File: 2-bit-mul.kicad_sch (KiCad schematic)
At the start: 7 parts, among them U4 SN74LS08N, U6 SN74LS08N, U7 SN74LS08N, U8 SN74HC86N

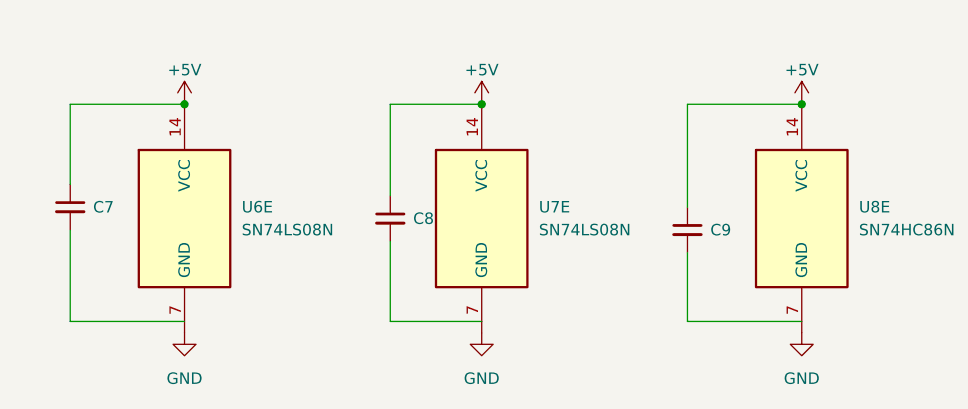
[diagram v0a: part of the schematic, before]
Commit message: fix: fixed link of capas
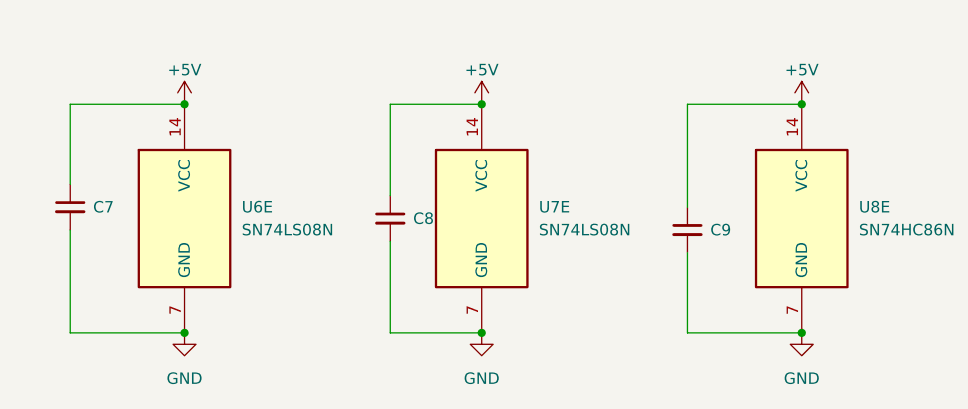
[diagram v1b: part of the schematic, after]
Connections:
- net GND: now also C7.2, C8.2, C9.2
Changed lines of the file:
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@@
+	)
+	(junction
+		(at 63.5 146.05)
+		(diameter 0)
+		(color 0 0 0 0)
 	)
 	(junction
@@
 	)
 	(junction
+		(at 96.52 146.05)
+		(diameter 0)
+		(color 0 0 0 0)
+	)
+	(junction
 		(at 132.08 120.65)
 		(diameter 0)
@@
 	(junction
 		(at 63.5 120.65)
+		(diameter 0)
+		(color 0 0 0 0)
+	)
+	(junction
+		(at 132.08 146.05)
 		(diameter 0)
 		(color 0 0 0 0)
@@
 	(wire
 		(pts
-			(xy 63.5 144.78) (xy 50.8 144.78)
+			(xy 119.38 137.16) (xy 119.38 146.05)
 		)
 		(stroke
@@
 	(wire
 		(pts
-			(xy 96.52 144.78) (xy 86.36 144.78)
-		)
-		(stroke
-			(width 0)
-			(type default)
-		)
-	)
-	(wire
-		(pts
-			(xy 119.38 144.78) (xy 119.38 137.16)
-		)
-		(stroke
-			(width 0)
-			(type default)
-		)
-	)
-	(wire
-		(pts
 			(xy 53.34 87.63) (xy 62.23 87.63)
 		)
@@
 	(wire
 		(pts
+			(xy 119.38 146.05) (xy 132.08 146.05)
+		)
+		(stroke
+			(width 0)
+			(type default)
+		)
+	)
+	(wire
+		(pts
 			(xy 63.5 93.98) (xy 67.31 93.98)
 		)
@@
 	(wire
 		(pts
-			(xy 86.36 144.78) (xy 86.36 135.89)
-		)
-		(stroke
-			(width 0)
-			(type default)
-		)
-	)
-	(wire
-		(pts
 			(xy 59.69 45.72) (xy 67.31 45.72)
 		)
@@
 	(wire
 		(pts
+			(xy 50.8 134.62) (xy 50.8 146.05)
+		)
+		(stroke
+			(width 0)
+			(type default)
+		)
+	)
+	(wire
+		(pts
 			(xy 123.19 87.63) (xy 132.08 87.63)
 		)
@@
 	(wire
 		(pts
+			(xy 86.36 135.89) (xy 86.36 146.05)
+		)
+		(stroke
+			(width 0)
+			(type default)
+		)
+	)
+	(wire
+		(pts
+			(xy 86.36 146.05) (xy 96.52 146.05)
+		)
+		(stroke
+			(width 0)
+			(type default)
+		)
+	)
+	(wire
+		(pts
 			(xy 86.36 80.01) (xy 88.9 80.01)
 		)
@@
 	(wire
 		(pts
-			(xy 132.08 144.78) (xy 119.38 144.78)
-		)
-		(stroke
-			(width 0)
-			(type default)
-		)
-	)
-	(wire
-		(pts
 			(xy 83.82 85.09) (xy 88.9 85.09)
 		)
@@
 	(wire
 		(pts
-			(xy 50.8 144.78) (xy 50.8 134.62)
-		)
-		(stroke
-			(width 0)
-			(type default)
-		)
-	)
-	(wire
-		(pts
 			(xy 62.23 40.64) (xy 67.31 40.64)
 		)
@@
 		)
 		(stroke
+			(width 0)
+			(type default)
+		)
+	)
+	(wire
+		(pts
+			(xy 50.8 146.05) (xy 63.5 146.05)
+		)
+		(stroke

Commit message: feat: updated references
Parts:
- C7, C8, C9: value C_Small -> CC0603KRX7R9BB104
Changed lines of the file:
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@@
 			)
 		)
-		(property "Value" "C_Small"
+		(property "Value" "CC0603KRX7R9BB104"
 			(at 121.92 135.8962 0)
 			(hide yes)
@@
 			)
 		)
-		(property "Value" "C_Small"
+		(property "Value" "CC0603KRX7R9BB104"
 			(at 88.9 134.6262 0)
 			(hide yes)
@@
 			)
 		)
-		(property "Value" "C_Small"
+		(property "Value" "CC0603KRX7R9BB104"
 			(at 53.34 133.3562 0)
 			(hide yes)

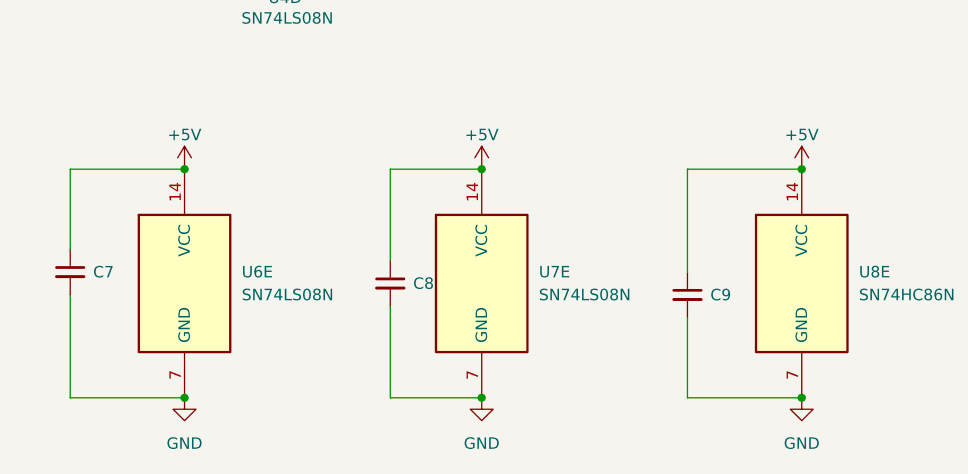
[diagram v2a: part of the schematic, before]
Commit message: Remove capacitors + change R and C footprints + finish PCB routing
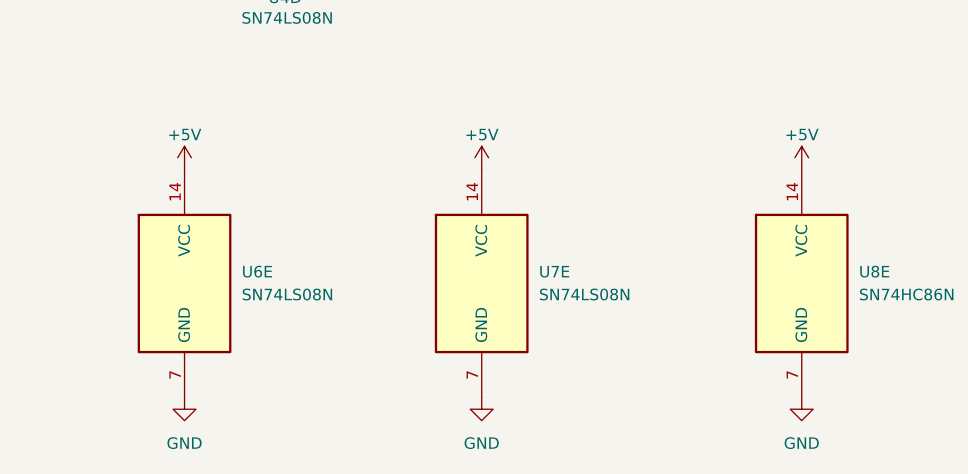
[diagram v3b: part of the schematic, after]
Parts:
- removed C7, C8, C9: CC0603KRX7R9BB104, Capacitor_SMD:C_0603_1608Metric_Pad1.08x0.95mm_HandSolder, symbol Device:C_Small

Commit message: fix: reput capas -- where is my gift?
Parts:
- added C7, C8, C9: C_Small, Capacitor_SMD:C_0603_1608Metric, symbol Device:C_Small
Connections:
- net +5V: now also C7.1, C8.1, C9.1
- net GND: now also C7.2, C8.2, C9.2
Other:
- moved on the sheet: U6E, U8E

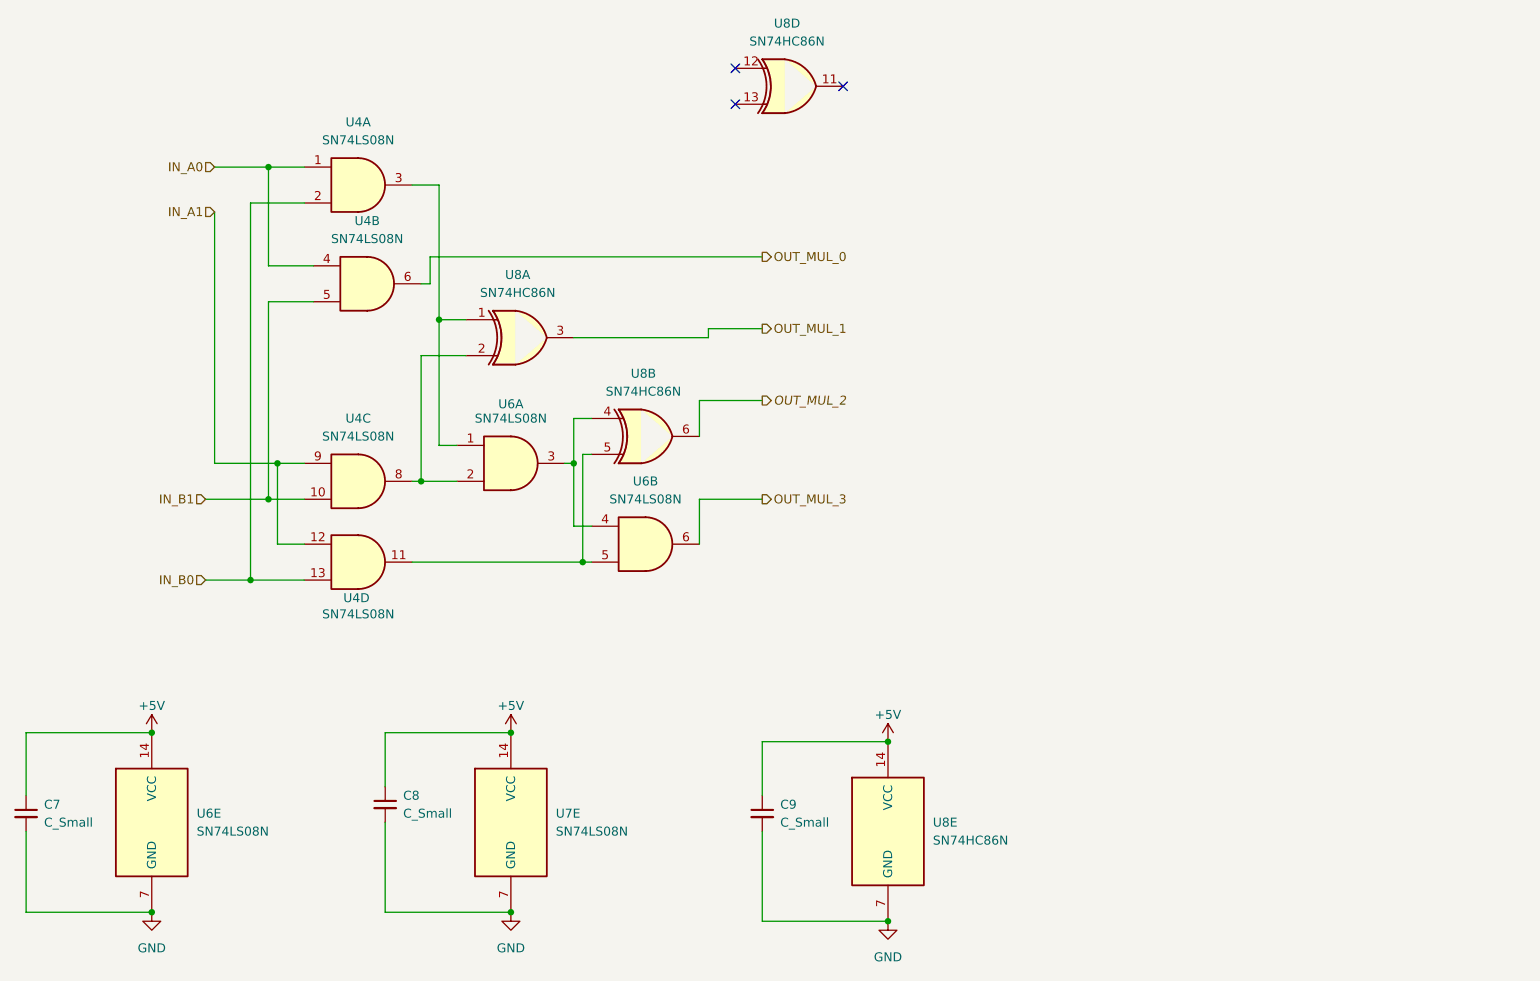
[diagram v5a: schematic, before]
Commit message: feat: multiplier schema
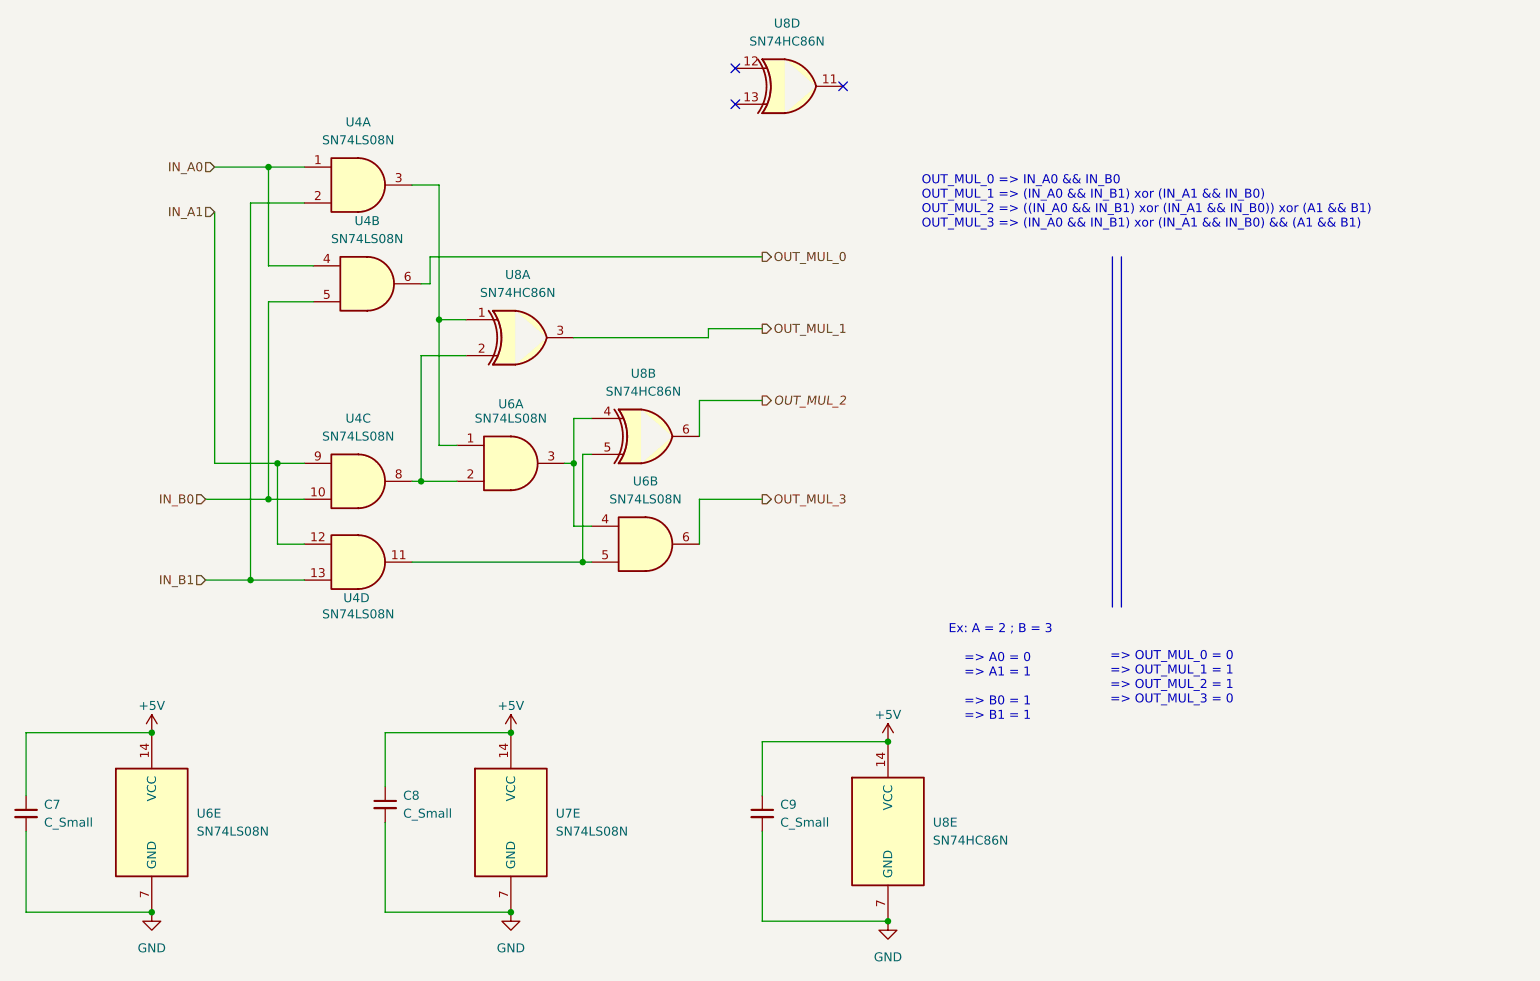
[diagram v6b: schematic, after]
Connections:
- net IN_B0: now also U4.10, U4.5; no longer U4.13, U4.2
- net IN_B1: now also U4.13, U4.2; no longer U4.10, U4.5

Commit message: feat: added point_tests + fixed wrong footprint for switch + added anime girl
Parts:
- added OUT_MUL_0, OUT_MUL_1, OUT_MUL_2, OUT_MUL_3: TestPoint, TestPoint:TestPoint_THTPad_D1.0mm_Drill0.5mm, symbol Connector:TestPoint
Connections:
- net OUT_MUL_0: now also OUT_MUL_0.1
- net OUT_MUL_1: now also OUT_MUL_1.1
- net OUT_MUL_2: now also OUT_MUL_2.1
- net OUT_MUL_3: now also OUT_MUL_3.1
